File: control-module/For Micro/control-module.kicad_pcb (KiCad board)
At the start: 2 copper layers, 63.5 x 68.1 mm, 28 parts, among them J1 For Expansion, J2 For Light Sensor, J3 From Solar Panel, J4 To Flow Module (F), J5 For Flow Module b, U1 TR_SERIES, U2 TR_SERIES, U3 ARDUINO_MICRO_SHIELD

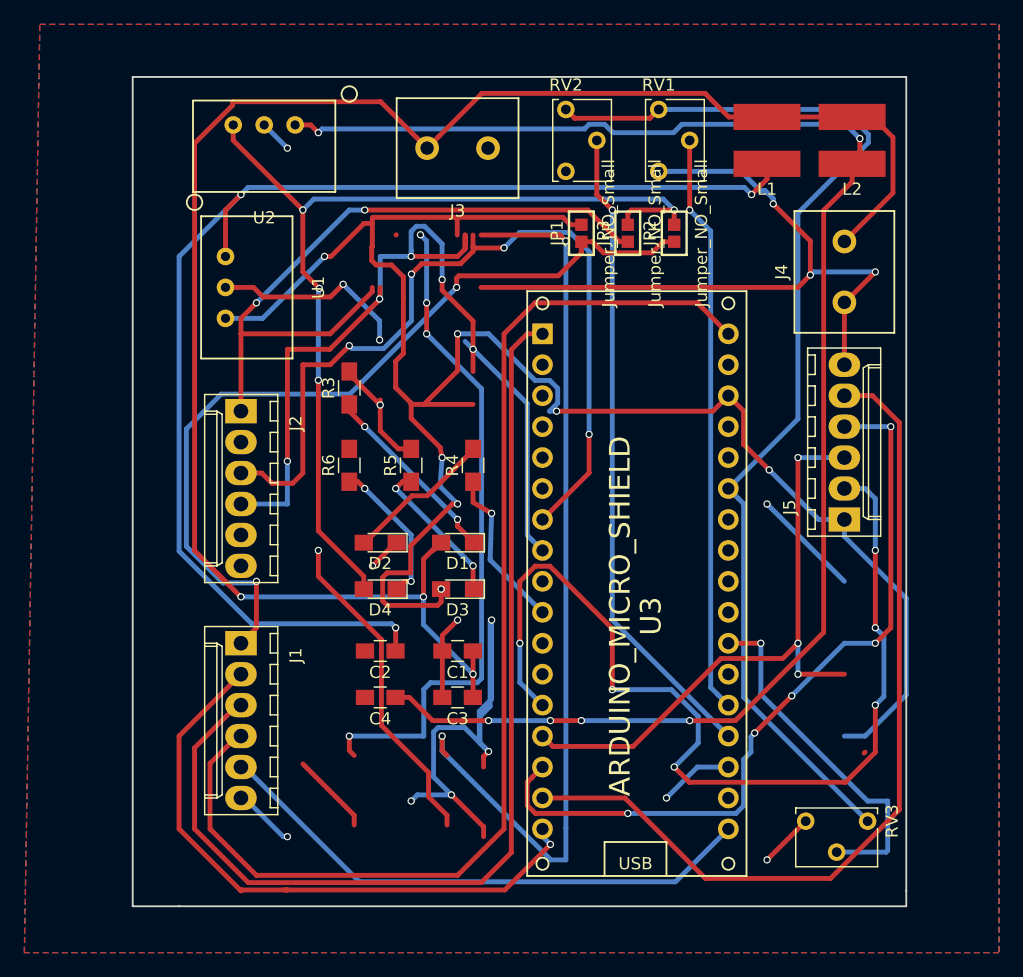
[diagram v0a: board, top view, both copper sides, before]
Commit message: Added ground planes and remove unnecessary tracks
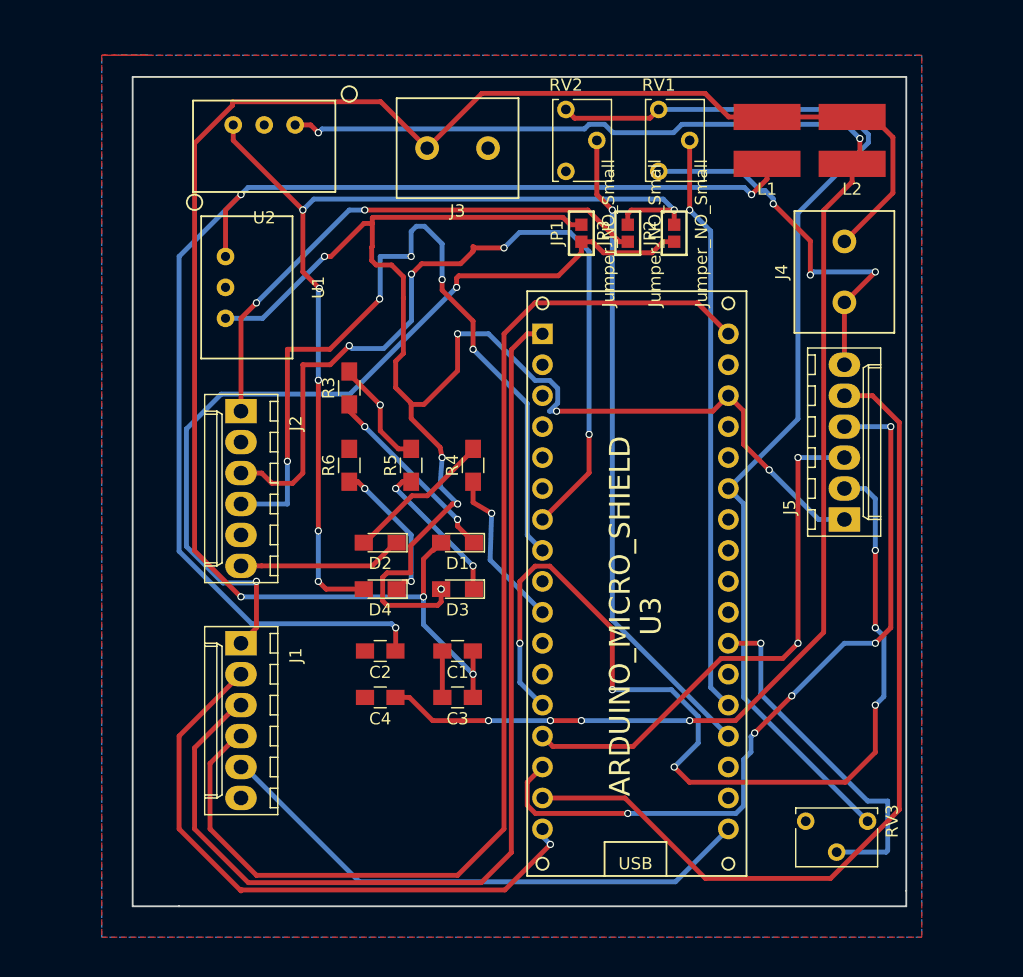
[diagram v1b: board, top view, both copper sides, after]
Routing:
- net (no net): track 216.6 -> 0.00 mm, vias 12 -> 0
- net GND: track 113.3 -> 58.9 mm, vias 12 -> 4
- net VCC+5V: track 157.6 -> 129.2 mm
- net VCC+LS: track 56.7 -> 44.1 mm
- net SCLA: track 76.7 -> 66.2 mm
- net INPUT3: track 50.2 -> 43.9 mm, vias 3 -> 2
- net VCC+3V: track 79.9 -> 81.7 mm, vias 4 -> 6
- net SDAA: track 70.9 -> 69.9 mm
- net 12V: track 146.6 -> 145.7 mm
